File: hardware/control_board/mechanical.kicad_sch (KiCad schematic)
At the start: 5 parts

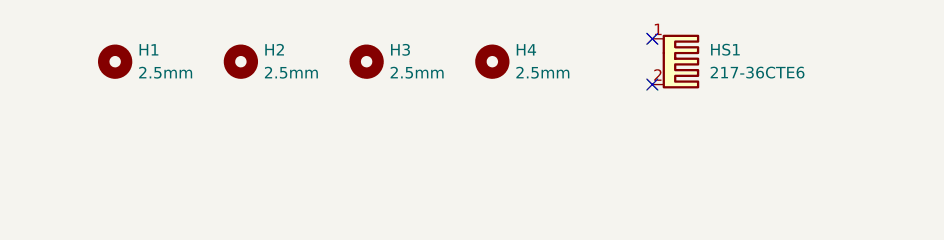
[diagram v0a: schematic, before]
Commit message: Route control board PCB tracks
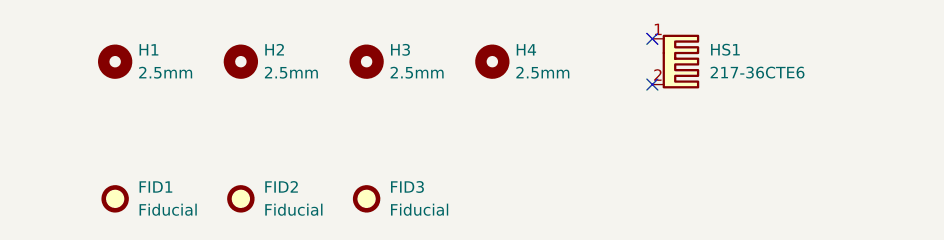
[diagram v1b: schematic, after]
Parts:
- added FID1, FID2, FID3: Fiducial, Fiducial:Fiducial_0.5mm_Mask1mm, symbol Mechanical:Fiducial
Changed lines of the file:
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@@
   (no_connect (at 175.26 97.79))
   (no_connect (at 175.26 102.87))
+  (symbol (lib_id "Mechanical:Fiducial") (at 129.54 115.57 0) (unit 1)
+    (in_bom yes) (on_board yes) (dnp no) (fields_autoplaced)
+    (property "Reference" "FID2" (at 132.08 114.3 0)
+      (effects (font (size 1.27 1.27)) (justify left))
+    )
+    (property "Value" "Fiducial" (at 132.08 116.84 0)
+      (effects (font (size 1.27 1.27)) (justify left))
+    )
+    (property "Footprint" "Fiducial:Fiducial_0.5mm_Mask1mm" (at 129.54 115.57 0)
+      (effects (font (size 1.27 1.27)) hide)
+    )
+    (property "Datasheet" "~" (at 129.54 115.57 0)
+      (effects (font (size 1.27 1.27)) hide)
+    )
+    (instances
+      (project "control_board"
+        (path "/b652b05a-4e3d-4ad1-b032-18886abe7d45/40a49d34-8d3e-4ffa-9e6c-b9f3c89d1a52"
+          (reference "FID2") (unit 1)
+        )
+      )
+    )
+  )
   (symbol (lib_id "Mechanical:MountingHole") (at 157.48 100.33 0) (unit 1)
     (in_bom no) (on_board yes) (dnp no) (fields_autoplaced)
@@
         )
       )
+    )
+  )
+  (symbol (lib_id "Mechanical:Fiducial") (at 115.57 115.57 0) (unit 1)
+    (in_bom yes) (on_board yes) (dnp no) (fields_autoplaced)
+    (property "Reference" "FID1" (at 118.11 114.3 0)
+      (effects (font (size 1.27 1.27)) (justify left))
+    )
+    (property "Value" "Fiducial" (at 118.11 116.84 0)
+      (effects (font (size 1.27 1.27)) (justify left))
+    )
+    (property "Footprint" "Fiducial:Fiducial_0.5mm_Mask1mm" (at 115.57 115.57 0)
+      (effects (font (size 1.27 1.27)) hide)
+    )
+    (property "Datasheet" "~" (at 115.57 115.57 0)
+      (effects (font (size 1.27 1.27)) hide)
+    )
+    (instances
+      (project "control_board"
+        (path "/b652b05a-4e3d-4ad1-b032-18886abe7d45/40a49d34-8d3e-4ffa-9e6c-b9f3c89d1a52"
+          (reference "FID1") (unit 1)
+        )
+      )
+    )
+  )
+  (symbol (lib_id "Mechanical:Fiducial") (at 143.51 115.57 0) (unit 1)
+    (in_bom yes) (on_board yes) (dnp no) (fields_autoplaced)
+    (property "Reference" "FID3" (at 146.05 114.3 0)
+      (effects (font (size 1.27 1.27)) (justify left))
+    )
+    (property "Value" "Fiducial" (at 146.05 116.84 0)
+      (effects (font (size 1.27 1.27)) (justify left))
+    )
+    (property "Footprint" "Fiducial:Fiducial_0.5mm_Mask1mm" (at 143.51 115.57 0)
+      (effects (font (size 1.27 1.27)) hide)
+    )
+    (property "Datasheet" "~" (at 143.51 115.57 0)
+      (effects (font (size 1.27 1.27)) hide)
+    )
+    (instances
+      (project "control_board"
+        (path "/b652b05a-4e3d-4ad1-b032-18886abe7d45/40a49d34-8d3e-4ffa-9e6c-b9f3c89d1a52"
+          (reference "FID3") (unit 1)
+        )
+      )

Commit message: Minor layout adjustments
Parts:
- FID1, FID2, FID3: now left out of the parts list
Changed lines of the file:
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@@
   (no_connect (at 175.26 102.87))
   (symbol (lib_id "Mechanical:Fiducial") (at 129.54 115.57 0) (unit 1)
-    (in_bom yes) (on_board yes) (dnp no) (fields_autoplaced)
+    (in_bom no) (on_board yes) (dnp no) (fields_autoplaced)
     (property "Reference" "FID2" (at 132.08 114.3 0)
       (effects (font (size 1.27 1.27)) (justify left))
@@
   )
   (symbol (lib_id "Mechanical:Fiducial") (at 115.57 115.57 0) (unit 1)
-    (in_bom yes) (on_board yes) (dnp no) (fields_autoplaced)
+    (in_bom no) (on_board yes) (dnp no) (fields_autoplaced)
     (property "Reference" "FID1" (at 118.11 114.3 0)
       (effects (font (size 1.27 1.27)) (justify left))
@@
   )
   (symbol (lib_id "Mechanical:Fiducial") (at 143.51 115.57 0) (unit 1)
-    (in_bom yes) (on_board yes) (dnp no) (fields_autoplaced)
+    (in_bom no) (on_board yes) (dnp no) (fields_autoplaced)
     (property "Reference" "FID3" (at 146.05 114.3 0)
       (effects (font (size 1.27 1.27)) (justify left))

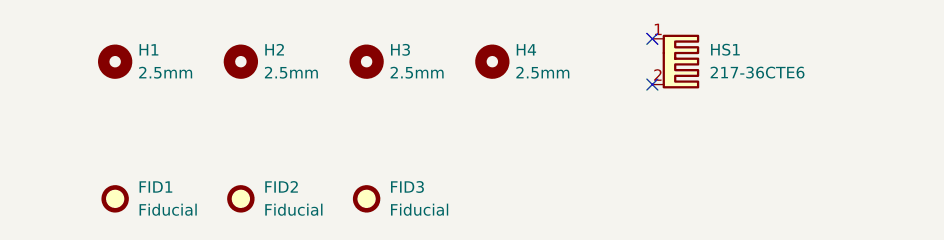
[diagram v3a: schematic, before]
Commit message: Adjust fiducials
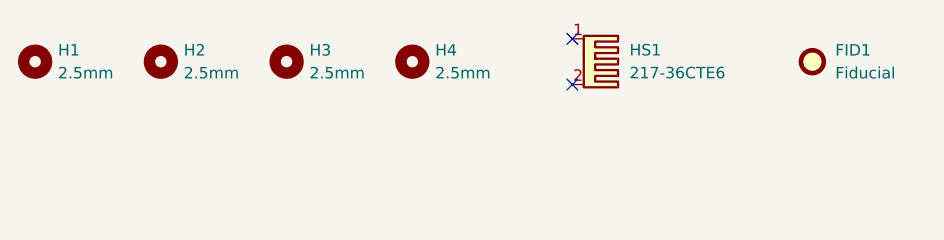
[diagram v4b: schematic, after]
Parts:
- removed FID2, FID3: Fiducial, Fiducial:Fiducial_0.5mm_Mask1mm, symbol Mechanical:Fiducial
- FID1: footprint Fiducial:Fiducial_0.5mm_Mask1mm -> Fiducial:Fiducial_1mm_Mask2mm
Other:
- moved on the sheet: FID1, H1, H2, H3, H4, HS1
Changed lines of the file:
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@@
   (paper "A4")
   (title_block
+    (date "2023-11-13")
     (rev "${REVISION}")
     (company "Author: I. Kajdan")
     (comment 1 "Promoter: A. Bondyra, Ph.D.")
   )
-  (no_connect (at 175.26 97.79))
-  (no_connect (at 175.26 102.87))
-  (symbol (lib_id "Mechanical:Fiducial") (at 129.54 115.57 0) (unit 1)
+  (no_connect (at 166.37 97.79))
+  (no_connect (at 166.37 102.87))
+  (symbol (lib_id "Mechanical:MountingHole") (at 148.59 100.33 0) (unit 1)
     (in_bom no) (on_board yes) (dnp no) (fields_autoplaced)
-    (property "Reference" "FID2" (at 132.08 114.3 0)
+    (property "Reference" "H4" (at 151.13 99.06 0)
       (effects (font (size 1.27 1.27)) (justify left))
     )
-    (property "Value" "Fiducial" (at 132.08 116.84 0)
+    (property "Value" "2.5mm" (at 151.13 101.6 0)
       (effects (font (size 1.27 1.27)) (justify left))
     )
-    (property "Footprint" "Fiducial:Fiducial_0.5mm_Mask1mm" (at 129.54 115.57 0)
+    (property "Footprint" "MountingHole:MountingHole_2.5mm" (at 148.59 100.33 0)
       (effects (font (size 1.27 1.27)) hide)
     )
-    (property "Datasheet" "~" (at 129.54 115.57 0)
-      (effects (font (size 1.27 1.27)) hide)
-    )
-    (instances
-      (project "control_board"
-        (path "/b652b05a-4e3d-4ad1-b032-18886abe7d45/40a49d34-8d3e-4ffa-9e6c-b9f3c89d1a52"
-          (reference "FID2") (unit 1)
-        )
-      )
-    )
-  )
-  (symbol (lib_id "Mechanical:MountingHole") (at 157.48 100.33 0) (unit 1)
-    (in_bom no) (on_board yes) (dnp no) (fields_autoplaced)
-    (property "Reference" "H4" (at 160.02 99.06 0)
-      (effects (font (size 1.27 1.27)) (justify left))
-    )
-    (property "Value" "2.5mm" (at 160.02 101.6 0)
-      (effects (font (size 1.27 1.27)) (justify left))
-    )
-    (property "Footprint" "MountingHole:MountingHole_2.5mm" (at 157.48 100.33 0)
-      (effects (font (size 1.27 1.27)) hide)
-    )
-    (property "Datasheet" "~" (at 157.48 100.33 0)
+    (property "Datasheet" "~" (at 148.59 100.33 0)
       (effects (font (size 1.27 1.27)) hide)
     )
@@
     )
   )
-  (symbol (lib_id "Mechanical:MountingHole") (at 143.51 100.33 0) (unit 1)
+  (symbol (lib_id "Mechanical:MountingHole") (at 134.62 100.33 0) (unit 1)
     (in_bom no) (on_board yes) (dnp no) (fields_autoplaced)
-    (property "Reference" "H3" (at 146.05 99.06 0)
+    (property "Reference" "H3" (at 137.16 99.06 0)
       (effects (font (size 1.27 1.27)) (justify left))
     )
-    (property "Value" "2.5mm" (at 146.05 101.6 0)
+    (property "Value" "2.5mm" (at 137.16 101.6 0)
       (effects (font (size 1.27 1.27)) (justify left))
     )
-    (property "Footprint" "MountingHole:MountingHole_2.5mm" (at 143.51 100.33 0)
+    (property "Footprint" "MountingHole:MountingHole_2.5mm" (at 134.62 100.33 0)
       (effects (font (size 1.27 1.27)) hide)
     )
-    (property "Datasheet" "~" (at 143.51 100.33 0)
+    (property "Datasheet" "~" (at 134.62 100.33 0)
       (effects (font (size 1.27 1.27)) hide)
     )
@@
     )
   )
-  (symbol (lib_id "Mechanical:MountingHole") (at 115.57 100.33 0) (unit 1)
+  (symbol (lib_id "Mechanical:MountingHole") (at 106.68 100.33 0) (unit 1)
     (in_bom no) (on_board yes) (dnp no) (fields_autoplaced)
-    (property "Reference" "H1" (at 118.11 99.06 0)
+    (property "Reference" "H1" (at 109.22 99.06 0)
       (effects (font (size 1.27 1.27)) (justify left))
     )
-    (property "Value" "2.5mm" (at 118.11 101.6 0)
+    (property "Value" "2.5mm" (at 109.22 101.6 0)
       (effects (font (size 1.27 1.27)) (justify left))
     )
-    (property "Footprint" "MountingHole:MountingHole_2.5mm" (at 115.57 100.33 0)
+    (property "Footprint" "MountingHole:MountingHole_2.5mm" (at 106.68 100.33 0)
       (effects (font (size 1.27 1.27)) hide)
     )
-    (property "Datasheet" "~" (at 115.57 100.33 0)
+    (property "Datasheet" "~" (at 106.68 100.33 0)
       (effects (font (size 1.27 1.27)) hide)
     )
@@
     )
   )
-  (symbol (lib_id "Mechanical:Heatsink_Pad_2Pin") (at 177.8 100.33 270) (unit 1)
+  (symbol (lib_id "Mechanical:Heatsink_Pad_2Pin") (at 168.91 100.33 270) (unit 1)
     (in_bom yes) (on_board yes) (dnp no) (fields_autoplaced)
-    (property "Reference" "HS1" (at 181.61 99.0473 90)
+    (property "Reference" "HS1" (at 172.72 99.0473 90)
       (effects (font (size 1.27 1.27)) (justify left))
     )
-    (property "Value" "217-36CTE6" (at 181.61 101.5873 90)
+    (property "Value" "217-36CTE6" (at 172.72 101.5873 90)
       (effects (font (size 1.27 1.27)) (justify left))
     )
-    (property "Footprint" "Local_Library:217-36CTx6" (at 176.53 100.6348 0)
+    (property "Footprint" "Local_Library:217-36CTx6" (at 167.64 100.6348 0)
       (effects (font (size 1.27 1.27)) hide)
     )
-    (property "Datasheet" "https://www.mouser.pl/datasheet/2/433/217-844229.pdf" (at 176.53 100.6348 0)
+    (property "Datasheet" "https://www.mouser.pl/datasheet/2/433/217-844229.pdf" (at 167.64 100.6348 0)
       (effects (font (size 1.27 1.27)) hide)
     )
@@
     )
   )
-  (symbol (lib_id "Mechanical:Fiducial") (at 115.57 115.57 0) (unit 1)
+  (symbol (lib_id "Mechanical:Fiducial") (at 193.04 100.33 0) (unit 1)
     (in_bom no) (on_board yes) (dnp no) (fields_autoplaced)
-    (property "Reference" "FID1" (at 118.11 114.3 0)
+    (property "Reference" "FID1" (at 195.58 99.06 0)
       (effects (font (size 1.27 1.27)) (justify left))
     )
-    (property "Value" "Fiducial" (at 118.11 116.84 0)
+    (property "Value" "Fiducial" (at 195.58 101.6 0)
       (effects (font (size 1.27 1.27)) (justify left))
     )
-    (property "Footprint" "Fiducial:Fiducial_0.5mm_Mask1mm" (at 115.57 115.57 0)
+    (property "Footprint" "Fiducial:Fiducial_1mm_Mask2mm" (at 193.04 100.33 0)
       (effects (font (size 1.27 1.27)) hide)
     )
-    (property "Datasheet" "~" (at 115.57 115.57 0)
+    (property "Datasheet" "~" (at 193.04 100.33 0)
       (effects (font (size 1.27 1.27)) hide)
     )
@@
     )
   )
-  (symbol (lib_id "Mechanical:Fiducial") (at 143.51 115.57 0) (unit 1)
+  (symbol (lib_id "Mechanical:MountingHole") (at 120.65 100.33 0) (unit 1)
     (in_bom no) (on_board yes) (dnp no) (fields_autoplaced)
-    (property "Reference" "FID3" (at 146.05 114.3 0)
+    (property "Reference" "H2" (at 123.19 99.06 0)
       (effects (font (size 1.27 1.27)) (justify left))
     )
-    (property "Value" "Fiducial" (at 146.05 116.84 0)
+    (property "Value" "2.5mm" (at 123.19 101.6 0)
       (effects (font (size 1.27 1.27)) (justify left))
     )
-    (property "Footprint" "Fiducial:Fiducial_0.5mm_Mask1mm" (at 143.51 115.57 0)
+    (property "Footprint" "MountingHole:MountingHole_2.5mm" (at 120.65 100.33 0)
       (effects (font (size 1.27 1.27)) hide)
     )
-    (property "Datasheet" "~" (at 143.51 115.57 0)
+    (property "Datasheet" "~" (at 120.65 100.33 0)
       (effects (font (size 1.27 1.27)) hide)
     )
-    (instances
-      (project "control_board"
-        (path "/b652b05a-4e3d-4ad1-b032-18886abe7d45/40a49d34-8d3e-4ffa-9e6c-b9f3c89d1a52"
-          (reference "FID3") (unit 1)
-        )
-      )
-    )
-  )
-  (symbol (lib_id "Mechanical:MountingHole") (at 129.54 100.33 0) (unit 1)
-    (in_bom no) (on_board yes) (dnp no) (fields_autoplaced)
-    (property "Reference" "H2" (at 132.08 99.06 0)
-      (effects (font (size 1.27 1.27)) (justify left))
-    )
-    (property "Value" "2.5mm" (at 132.08 101.6 0)
-      (effects (font (size 1.27 1.27)) (justify left))
-    )
-    (property "Footprint" "MountingHole:MountingHole_2.5mm" (at 129.54 100.33 0)
-      (effects (font (size 1.27 1.27)) hide)
-    )
-    (property "Datasheet" "~" (at 129.54 100.33 0)
-      (effects (font (size 1.27 1.27)) hide)
-    )

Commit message: Update reference designators
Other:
- title: (none) -> Mechanical Components
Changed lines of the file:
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@@
   (paper "A4")
   (title_block
+    (title "Mechanical Components")
     (date "2023-11-29")
     (rev "${REVISION}")
@@
     (instances
       (project "control_board"
-        (path "/b652b05a-4e3d-4ad1-b032-18886abe7d45"
-          (reference "H4") (unit 1)
-        )
         (path "/b652b05a-4e3d-4ad1-b032-18886abe7d45/40a49d34-8d3e-4ffa-9e6c-b9f3c89d1a52"
           (reference "H4") (unit 1)
@@
     (instances
       (project "control_board"
-        (path "/b652b05a-4e3d-4ad1-b032-18886abe7d45"
-          (reference "H3") (unit 1)
-        )
         (path "/b652b05a-4e3d-4ad1-b032-18886abe7d45/40a49d34-8d3e-4ffa-9e6c-b9f3c89d1a52"
           (reference "H3") (unit 1)
@@
     (instances
       (project "control_board"
-        (path "/b652b05a-4e3d-4ad1-b032-18886abe7d45"
-          (reference "H1") (unit 1)
-        )
         (path "/b652b05a-4e3d-4ad1-b032-18886abe7d45/40a49d34-8d3e-4ffa-9e6c-b9f3c89d1a52"
           (reference "H1") (unit 1)
@@
     (instances
       (project "control_board"
-        (path "/b652b05a-4e3d-4ad1-b032-18886abe7d45/d341d3a2-ea4e-4772-851c-7c5b5be32855"
-          (reference "HS1") (unit 1)
-        )
         (path "/b652b05a-4e3d-4ad1-b032-18886abe7d45/40a49d34-8d3e-4ffa-9e6c-b9f3c89d1a52"
           (reference "HS1") (unit 1)
@@
     (instances
       (project "control_board"
-        (path "/b652b05a-4e3d-4ad1-b032-18886abe7d45"
-          (reference "H2") (unit 1)
-        )
         (path "/b652b05a-4e3d-4ad1-b032-18886abe7d45/40a49d34-8d3e-4ffa-9e6c-b9f3c89d1a52"
           (reference "H2") (unit 1)
